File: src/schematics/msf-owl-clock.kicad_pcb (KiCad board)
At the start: 4 copper layers, 130.1 x 183.6 mm, 446 parts, among them Q101 NX6008NBKW, Q301 NX6008NBKW, Q501 NX6008NBKW, Q502 NX6008NBKW, Q503 NX6008NBKW, Q504 NX6008NBKW, Q505 NX6008NBKW, Q601 NX6008NBKW, Q602 BC847BS, Q603 BC847BS, U001 BC805M, U002 TSOP75338TT, U101 MP5016HGQH, U102 BQ24392RSER, U103 FUSB302BMPX, U104 TPS628512DRLR, U201 TPS7A2040PDQNR, U202 TPS7A2036PDBVR, U203 MCP6499, U204 MCP6499, U205 74HC595BQ, U206 TMUX1511RSV, U207 TMUX1511RSV, U301 PIC32CX1025SG41100-I/E5X, U302 AP22653AW6, U401 AP22653AW6, U402 MCP6486U, U403 IS31AP4991A-SLS2, U501 TPS7A2028PDBVR, U502 DPS310XTSA1, U503 HDC3022, U504 VL6180V1NR1, U601 TMUX1574RSV, U602 TMUX1574RSV, U603 TMUX1574RSV

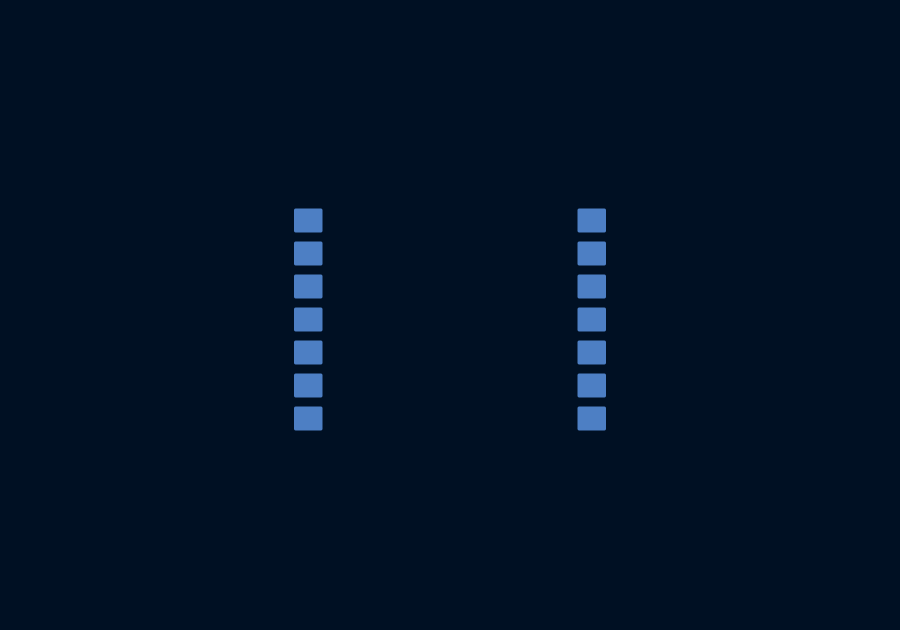
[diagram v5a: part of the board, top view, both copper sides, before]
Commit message: Added a DRC rule to set the board-to-fill distance independently of the [via|track|whatever]-to-fill distance.
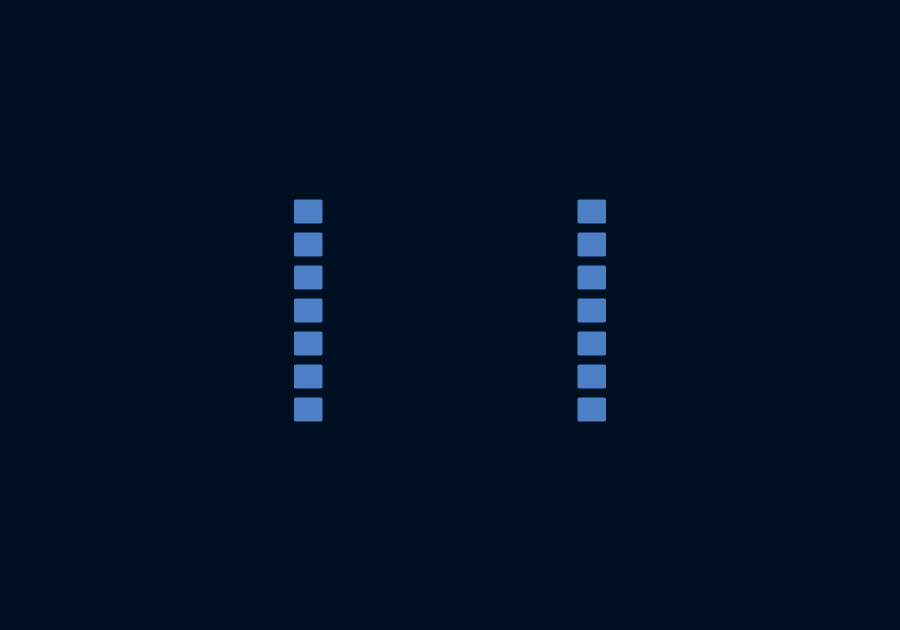
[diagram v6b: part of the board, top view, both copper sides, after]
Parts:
- moved U001 0.30 mm to (100.0, 42.2)
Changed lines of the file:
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@@
   )
   (footprint "restall-manufacturer-fanstel:BC805M" (layer "B.Cu")
-    (at 100 42.5 180)
+    (at 100 42.2 180)
     (descr "BC805M Bluetooth Low Energy (BLE 5.2) Module with Nordic nRF52805 SoC - 10.2mm x 14.3mm with 1.1mm Pitch (see https://www.fanstel.com/s/BC805M-p_Product-Specifications.pdf)")
     (tags "bc805m nrf nrf52805 bluetooth low energy ble 2.4ghz fanstel nordic")
@@
   (segment (start 136.26 96.2) (end 134.61 96.2) (width 0.1524) (layer "B.Cu") (net 283))
   (segment (start 134.61 95.1) (end 136.26 95.1) (width 0.1524) (layer "B.Cu") (net 284))
+  (zone (net 0) (net_name "") (layers "F.Cu" "In1.Cu" "In2.Cu" "B.Cu" "Edge.Cuts") (name "BluetoothAntennaKeepout") (hatch edge 0.5)
+    (connect_pads (clearance 0))
+    (min_thickness 0.25) (filled_areas_thickness no)
+    (keepout (tracks not_allowed) (vias not_allowed) (pads not_allowed) (copperpour not_allowed) (footprints allowed))
+    (fill (thermal_gap 0.5) (thermal_bridge_width 0.5))
+    (polygon
+      (pts
+        (xy 89.8 33)
+        (xy 110.2 33)
+        (xy 110.2 39.8)
+        (xy 89.8 39.8)
+      )
+    )
+  )
   (zone (net 73) (net_name "GND") (layer "In1.Cu") (name "GroundPlane1") (hatch edge 0.5)
     (connect_pads yes (clearance 0.5))
